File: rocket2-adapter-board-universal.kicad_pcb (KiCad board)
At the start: 2 copper layers, 45 x 66 mm, 10 parts, among them J1 DE15_Socket_HighDensity_Mount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

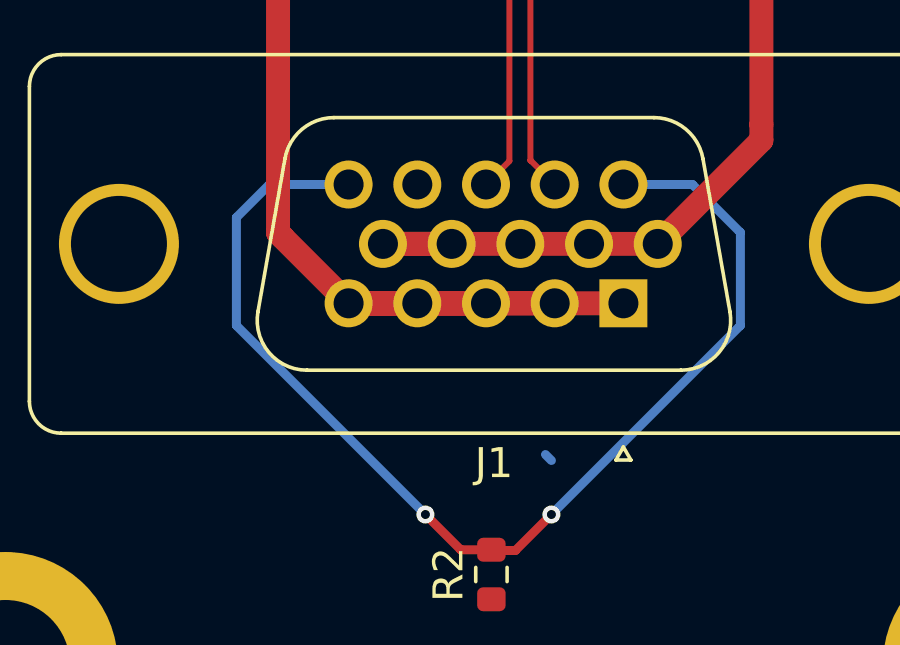
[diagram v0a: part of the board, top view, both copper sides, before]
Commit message: Quick Fix: Unconnected Pad
Added routing to a disconnected pad on pulldown pins
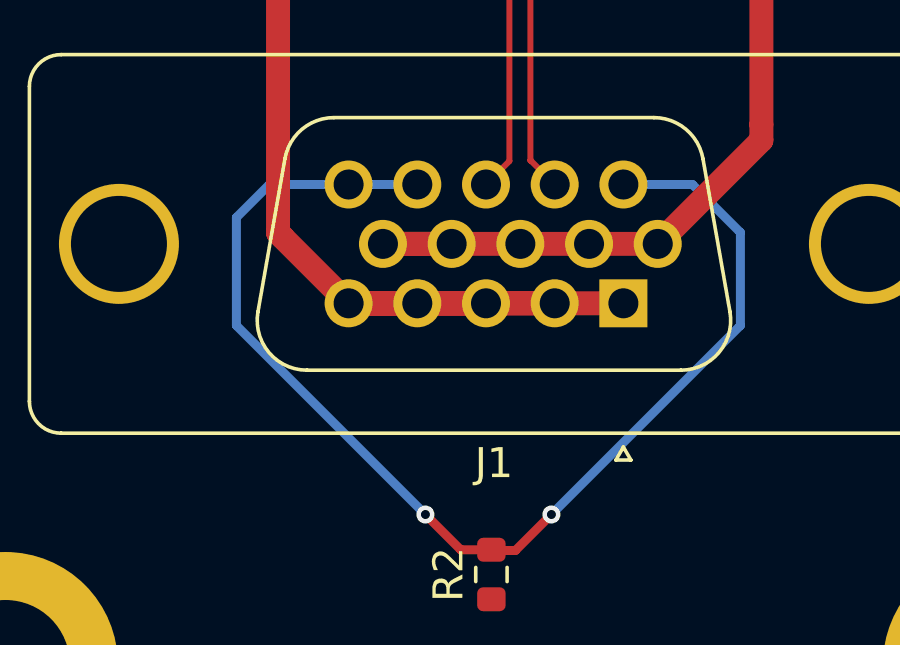
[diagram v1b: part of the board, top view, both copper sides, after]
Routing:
- net Net-(J1-Pad11): track 38.9 -> 40.9 mm
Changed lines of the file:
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@@
-	)
-	(segment
-		(start 144.2 113.2)
-		(end 144 113)
-		(width 0.3)
-		(layer "B.Cu")
-		(net 5)
 	)
 	(segment
@@
 		(start 134.8 104)
 		(end 133.7 105.1)
+		(width 0.3)
+		(layer "B.Cu")
+		(net 5)
+	)
+	(segment
+		(start 137.44 104)
+		(end 139.73 104)
 		(width 0.3)
 		(layer "B.Cu")
@@
 		(hatch edge 0.5)
 		(connect_pads
-			(clearance 0.5)
+			(clearance 0.1)
 		)
 		(min_thickness 0.25)
@@
 			(thermal_gap 0.5)
 			(thermal_bridge_width 0.5)
-			(island_removal_mode 1)
+			(island_removal_mode 2)
 			(island_area_min 10)
 		)
